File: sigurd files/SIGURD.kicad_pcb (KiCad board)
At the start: 4 copper layers, 70 x 70 mm, 117 parts, among them J1 INPUT, J10 24V Terminal, J11 12V/24V Terminal, J12 Extra NF, J2 CAN input, J3 CAN out (optional), J4 jst_sh 4, J5 Step Up Terminal, J6 PWM, J7 Motor Terminal, J8 Hall sensor, J9 12V Terminal, Q1 MMBT3904, U1 TCAN334GDCN, U2 STM32U575CGTx, U3 AMS1117-3.3, U4 LMR50410Y5FQDBVRQ1, U5 LMV324AIDR, U6 VN7050ASTR, U7 VN7050ASTR, U8 VN7050ASTR, Y1 48MHz

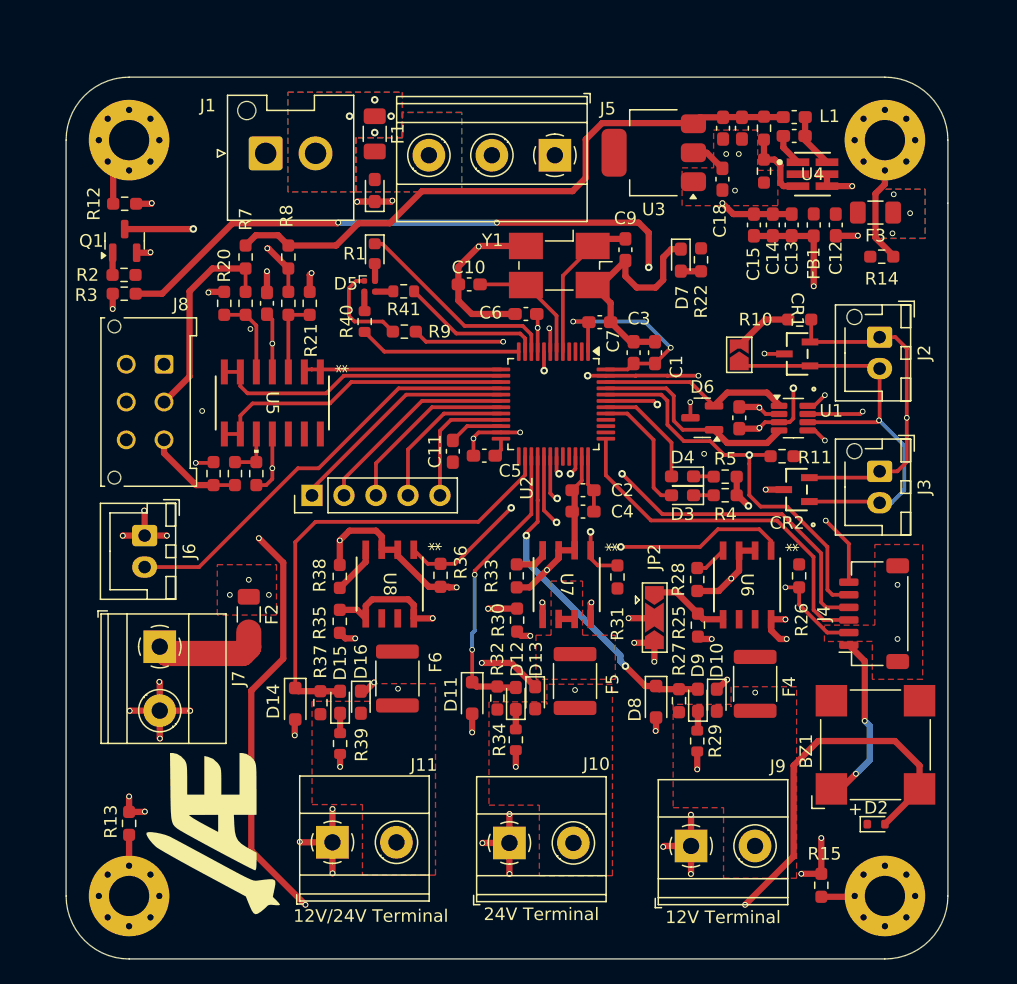
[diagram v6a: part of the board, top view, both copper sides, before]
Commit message: fixed pcb errors and most warnings
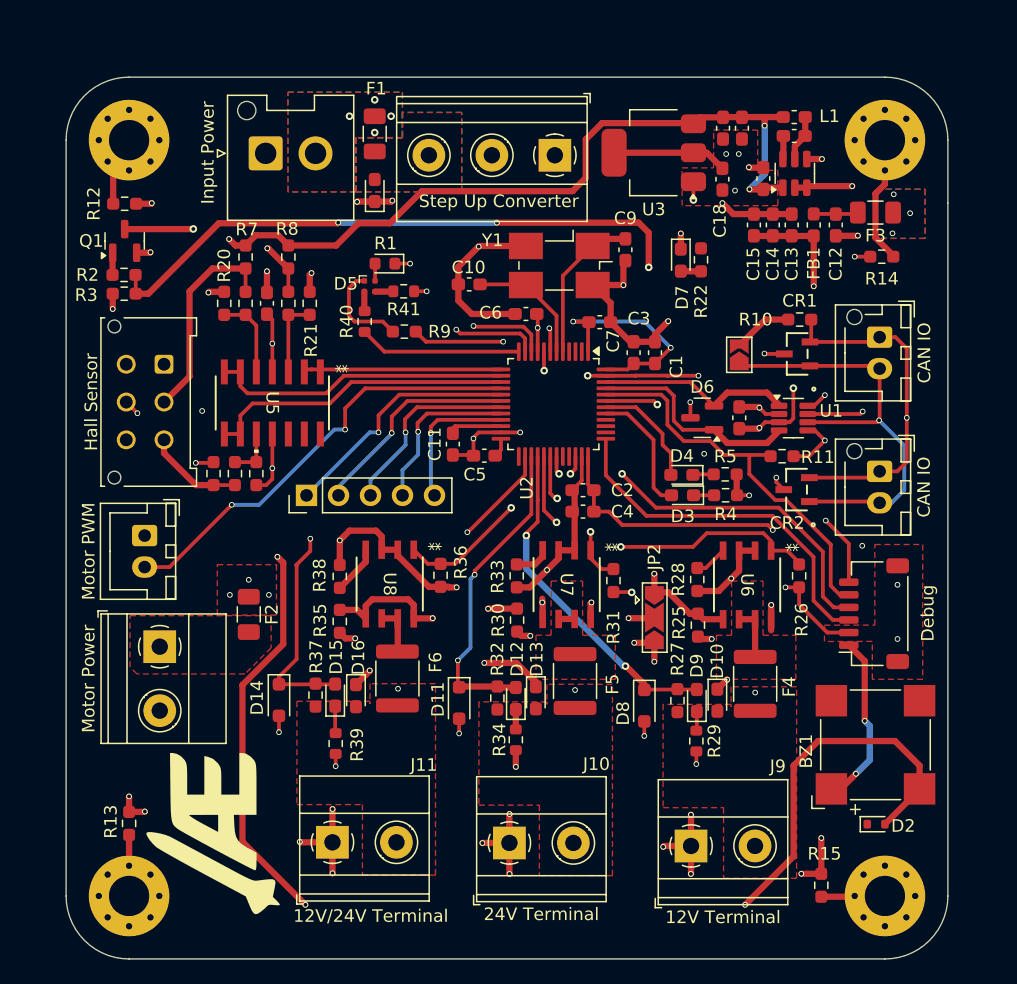
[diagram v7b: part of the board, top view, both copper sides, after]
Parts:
- removed R23: 88.7k, Resistor_SMD:R_0603_1608Metric_Pad0.98x0.95mm_HandSolder
- removed R24: 22.1k, Resistor_SMD:R_0603_1608Metric_Pad0.98x0.95mm_HandSolder
- removed U4: LMR50410Y5FQDBVRQ1, LMR50410Y5FQDBVRQ1:DBV0006A-IPC_A
- added C21: 22u, Capacitor_SMD:C_0603_1608Metric_Pad1.08x0.95mm_HandSolder, F.Cu at (125.3, 78.0)
- added U9: AP63205WU, Package_TO_SOT_SMD:TSOT-23-6, F.Cu at (127.8, 77.6)
- C14: value 1u -> 10u
- C16: value 10u -> 22u
- C19: value 0.1uF -> 0.1u
- CAN IO: renamed from J2
- CAN IO: renamed from J3
- Hall Sensor: renamed from J8
- Input Power: renamed from J1
- Motor PWM: renamed from J6
- Motor Power: renamed from J7
- Step Up Converter: renamed from J5
- moved D14 1.32 mm to (86.9, 119.5)
- moved R1 1.13 mm to (95.3, 84.8), turned to 180 degrees
- moved D11 1.11 mm to (101.2, 119.7)
- moved D8 0.98 mm to (115.9, 119.9)
- moved R37 0.72 mm to (89.8, 119.1)
- moved D15 0.69 mm to (91.4, 119.1)
- moved D16 0.65 mm to (93.0, 119.1)
- moved C11 0.57 mm to (100.7, 99.1)
- moved J12 0.44 mm to (89.1, 103.2)
- moved R31 0.43 mm to (113.5, 110.0)
- moved R39 0.35 mm to (91.4, 122.9)
- moved R5 0.18 mm to (122.3, 101.5)
- moved D4 0.13 mm to (118.9, 101.6)
- moved R27 0.12 mm to (118.5, 119.5)
- moved D9 0.09 mm to (120.1, 119.5)
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- renumbered J4 to Debug
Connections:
- C19 pad 1: Net-(U4-CB) -> Net-(U9-SW)
- C19 pad 2: Net-(U4-SW) -> Net-(U9-BST)
- L1 pad 1: Net-(U4-SW) -> Net-(U9-SW)
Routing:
- net 5V: track 55.4 -> 94.3 mm, vias 2 -> 6
- net +3V3: track 61.6 -> 90.4 mm, vias 7 -> 9
- net Net-(J7-Pin_1): track 8.92 -> 0.05 mm
- net Earth: track 187.2 -> 179.6 mm, vias 63 -> 64
- net Net-(U4-FB): track 5.97 -> 0.00 mm
- net Net-(U4-SW): track 4.30 -> 0.00 mm
- net Net-(F4-Pad2): track 0.00 -> 4.26 mm
- net Net-(F6-Pad2): track 0.00 -> 3.92 mm
- net Net-(U9-SW): track 0.00 -> 3.69 mm
- net Net-(C12-Pad2): track 0.00 -> 3.54 mm
- net Net-(U4-CB): track 2.56 -> 0.00 mm
- net /SOL1: track 25.2 -> 27.7 mm
- net Net-(U9-BST): track 0.00 -> 1.85 mm
- net /SOL2_SENSE: track 23.5 -> 25.3 mm
- net /LED_R: track 16.8 -> 15.0 mm, vias 0 -> 2
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- added copper zone on F.Cu, net Net-(F4-Pad2)
- added copper zone on F.Cu, net Net-(J7-Pin_1)
